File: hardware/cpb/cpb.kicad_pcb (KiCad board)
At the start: 6 copper layers, 95.9 x 90.2 mm, 5 parts, among them J1 Conn_02x20_Odd_Even

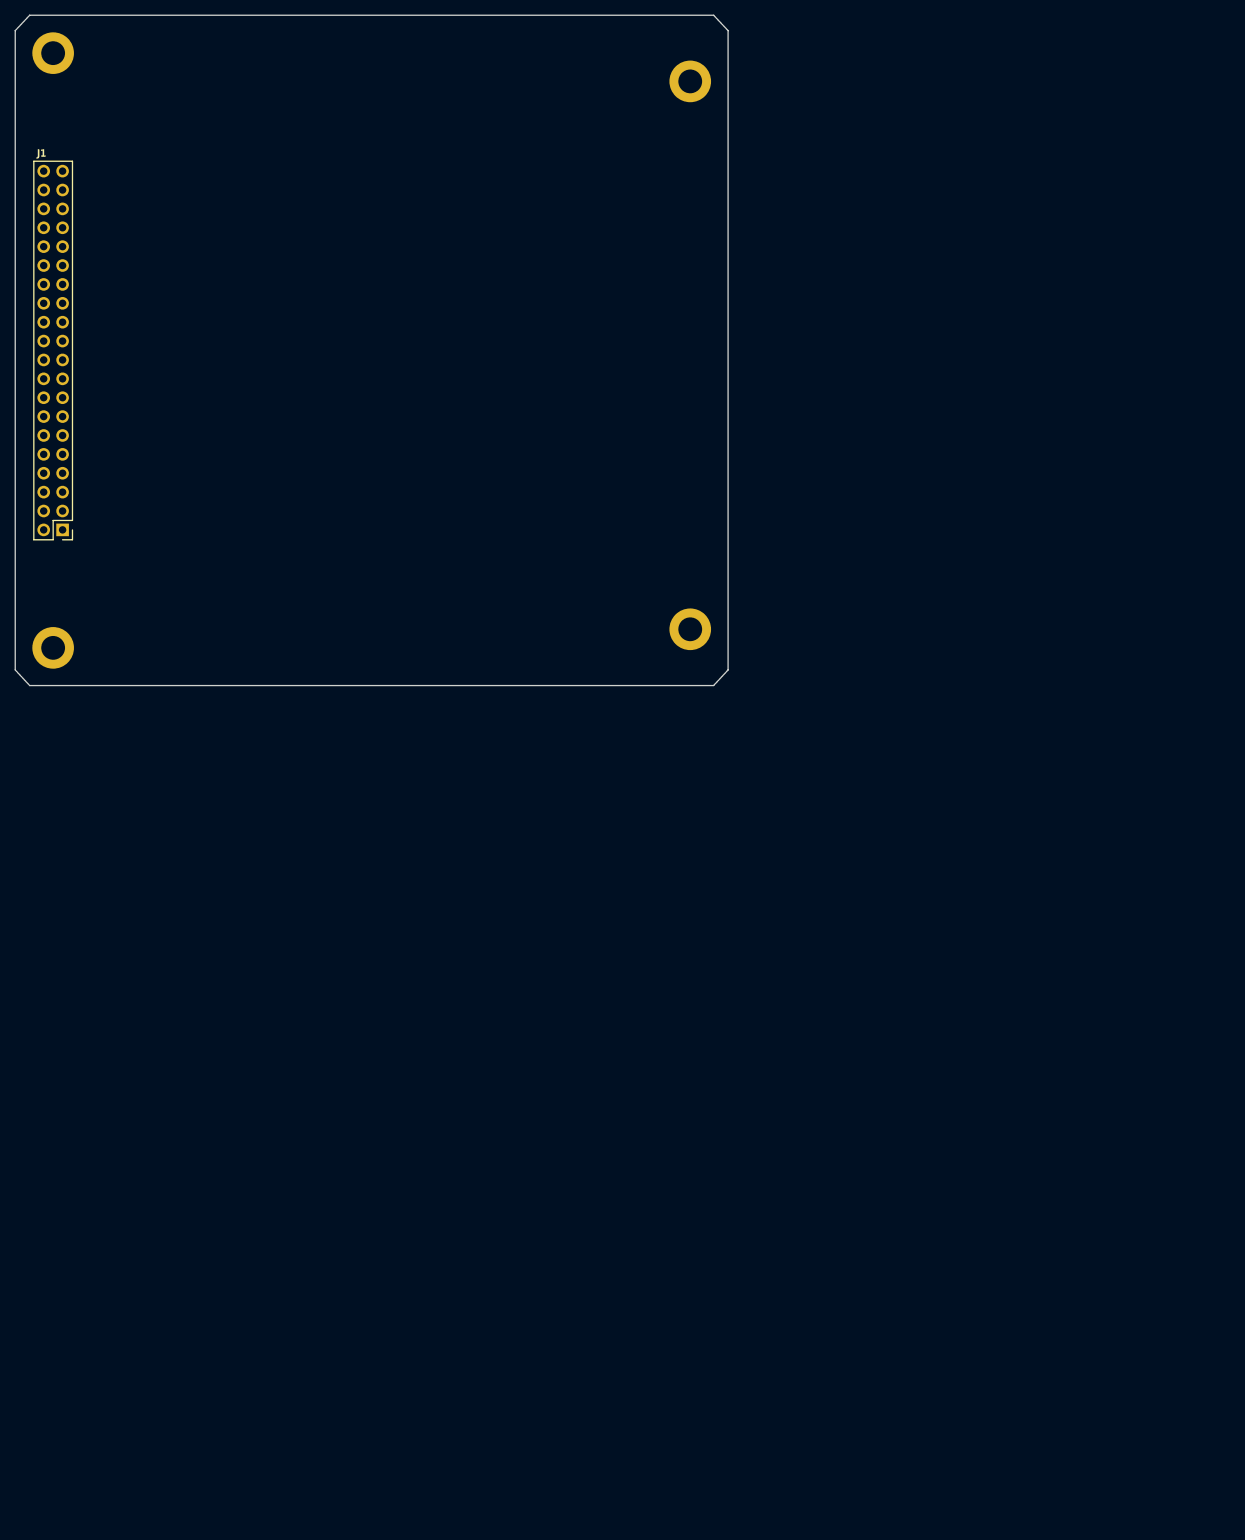
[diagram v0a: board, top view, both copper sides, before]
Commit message: hardware/cpb: Sorted initial ratsnest of CPB
This is the current revision of the sorted ratsnest of the CPB. Remaining tasks include placing down powerplanes as well as routing.
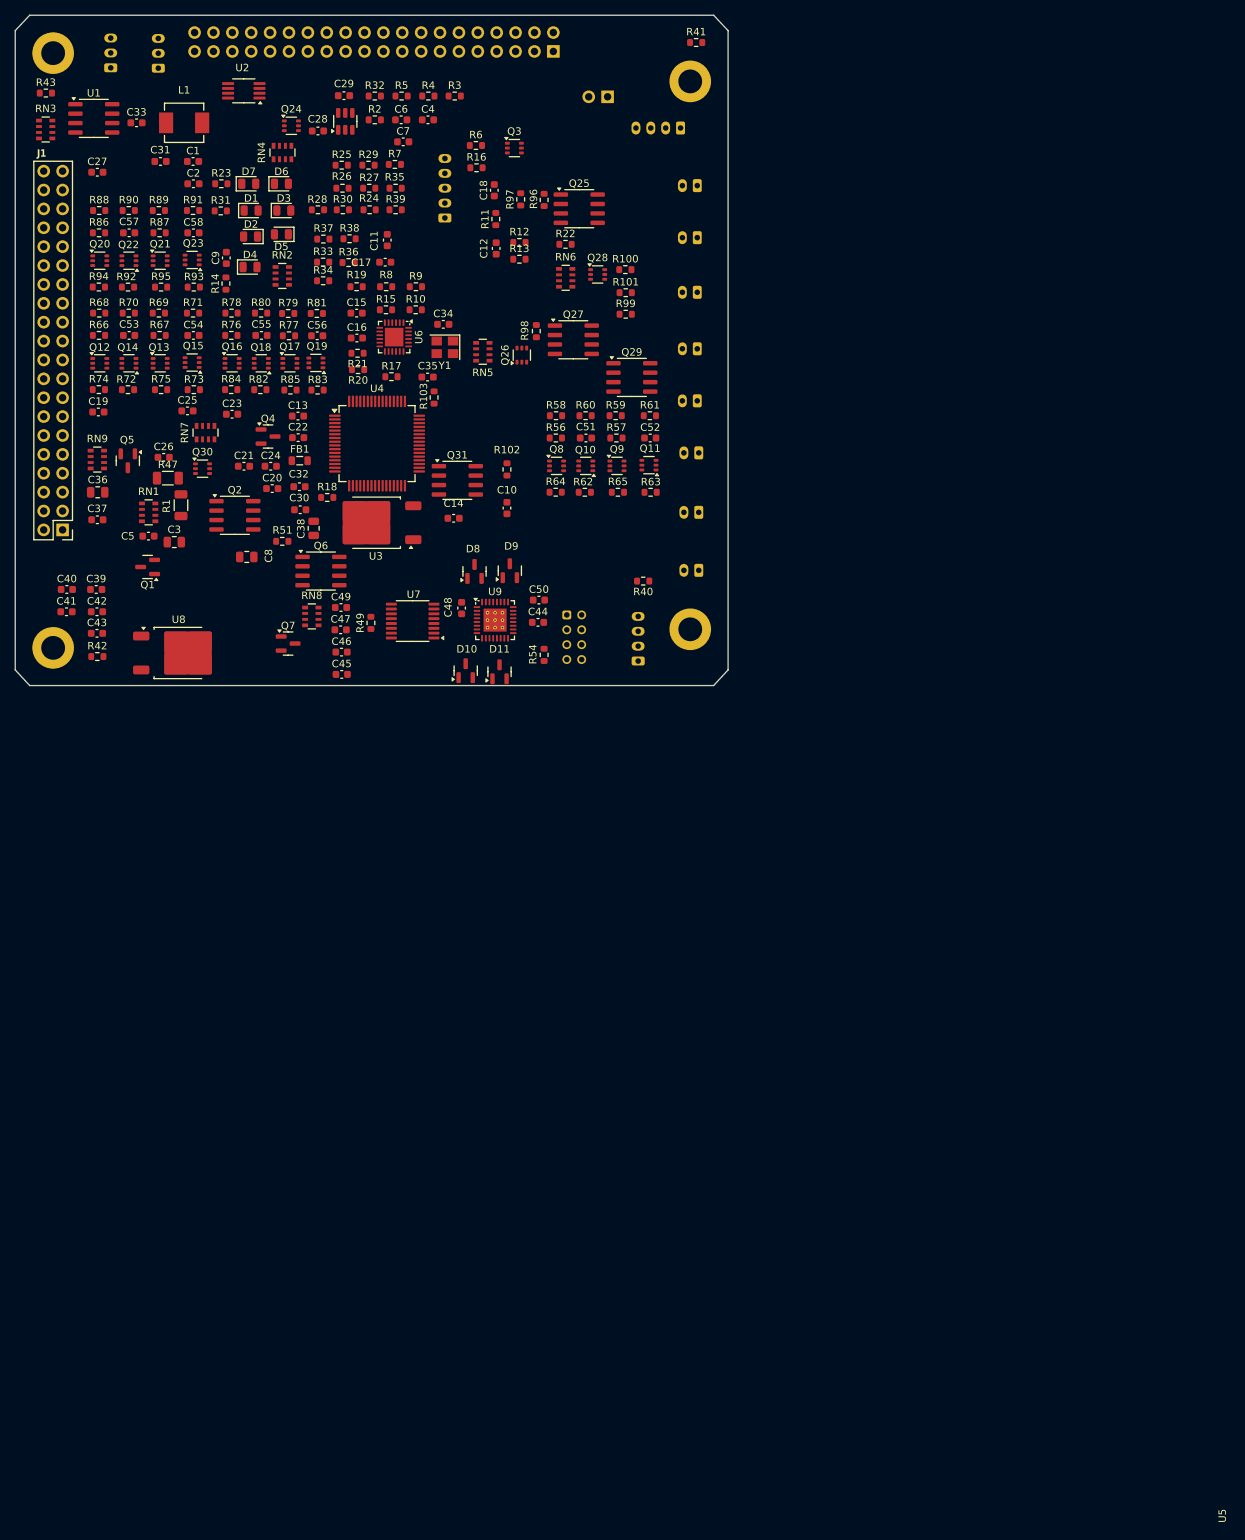
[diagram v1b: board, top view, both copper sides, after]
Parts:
- added C1: 100nF, Capacitor_SMD:C_0603_1608Metric, F.Cu at (124.8, 77.9)
- added C10: 2.2uF, Capacitor_SMD:C_0603_1608Metric, F.Cu at (167.0, 124.5)
- added C11: 68pF, Capacitor_SMD:C_0603_1608Metric, F.Cu at (150.9, 88.5)
- added C12: 68pF, Capacitor_SMD:C_0603_1608Metric, F.Cu at (165.6, 89.6)
- added C13: 100nF, Capacitor_SMD:C_0603_1608Metric, F.Cu at (138.9, 112.2)
- added C14: 100nF, Capacitor_SMD:C_0603_1608Metric, F.Cu at (159.8, 125.9)
- added C15: 100nF, Capacitor_SMD:C_0603_1608Metric, F.Cu at (146.8, 98.3)
- added C16: 100nF, Capacitor_SMD:C_0603_1608Metric, F.Cu at (146.8, 101.7)
- added C17: 10uF, Capacitor_SMD:C_0603_1608Metric, F.Cu at (150.6, 91.5)
- added C18: 10uF, Capacitor_SMD:C_0603_1608Metric, F.Cu at (165.3, 81.8)
- added C19: 100nF, Capacitor_SMD:C_0603_1608Metric, F.Cu at (112.0, 111.6)
- added C2: 100nF, Capacitor_SMD:C_0603_1608Metric, F.Cu at (124.8, 80.9)
- added C20: 100nF, Capacitor_SMD:C_0603_1608Metric, F.Cu at (135.4, 121.9)
- added C21: 100nF, Capacitor_SMD:C_0603_1608Metric, F.Cu at (131.6, 118.9)
- added C22: 100nF, Capacitor_SMD:C_0603_1608Metric, F.Cu at (138.9, 115.0)
- added C23: 100nF, Capacitor_SMD:C_0603_1608Metric, F.Cu at (130.0, 111.9)
- added C24: 100nF, Capacitor_SMD:C_0603_1608Metric, F.Cu at (135.2, 118.9)
- added C25: 100nF, Capacitor_SMD:C_0603_1608Metric, F.Cu at (124.0, 111.5)
- added C26: 100nF, Capacitor_SMD:C_0603_1608Metric, F.Cu at (120.8, 117.7)
- added C27: 100nF, Capacitor_SMD:C_0603_1608Metric, F.Cu at (111.9, 79.3)
- added C28: 2.2uF, Capacitor_SMD:C_0603_1608Metric, F.Cu at (141.6, 73.8)
- added C29: 100nF, Capacitor_SMD:C_0603_1608Metric, F.Cu at (145.1, 69.0)
- added C3: 22uF, Capacitor_SMD:C_0805_2012Metric, F.Cu at (122.2, 129.1)
- added C30: 100nF, Capacitor_SMD:C_0603_1608Metric, F.Cu at (139.2, 124.8)
- added C31: 2.2uF, Capacitor_SMD:C_0603_1608Metric, F.Cu at (120.4, 77.9)
- added C32: 2.2uF, Capacitor_SMD:C_0603_1608Metric, F.Cu at (139.1, 121.7)
- added C33: 100nF, Capacitor_SMD:C_0603_1608Metric, F.Cu at (117.2, 72.7)
- added C34: 22pF, Capacitor_SMD:C_0603_1608Metric, F.Cu at (158.4, 99.8)
- added C35: 15pF, Capacitor_SMD:C_0603_1608Metric, F.Cu at (156.3, 106.9)
- added C36: 22uF, Capacitor_SMD:C_0805_2012Metric, F.Cu at (112.0, 122.4)
- added C37: 2.2uF, Capacitor_SMD:C_0603_1608Metric, F.Cu at (111.9, 126.1)
- added C38: 22uF, Capacitor_SMD:C_0805_2012Metric, F.Cu at (141.0, 127.2)
- added C39: 2.2uF, Capacitor_SMD:C_0603_1608Metric, F.Cu at (111.8, 135.5)
- added C4: 100nF, Capacitor_SMD:C_0603_1608Metric, F.Cu at (156.4, 72.3)
- added C40: 100nF, Capacitor_SMD:C_0603_1608Metric, F.Cu at (107.8, 135.5)
- added C41: 100nF, Capacitor_SMD:C_0603_1608Metric, F.Cu at (107.8, 138.5)
- added C42: 100nF, Capacitor_SMD:C_0603_1608Metric, F.Cu at (111.8, 138.5)
- added C43: 100nF, Capacitor_SMD:C_0603_1608Metric, F.Cu at (111.8, 141.4)
- added C44: 2.2uF, Capacitor_SMD:C_0603_1608Metric, F.Cu at (171.2, 139.9)
- added C45: 100nF, Capacitor_SMD:C_0603_1608Metric, F.Cu at (144.8, 146.9)
- added C46: 100nF, Capacitor_SMD:C_0603_1608Metric, F.Cu at (144.8, 143.9)
- added C47: 100nF, Capacitor_SMD:C_0603_1608Metric, F.Cu at (144.6, 140.9)
- added C48: 1.0uF, Capacitor_SMD:C_0603_1608Metric, F.Cu at (160.9, 138.0)
- added C49: 100nF, Capacitor_SMD:C_0603_1608Metric, F.Cu at (144.7, 137.9)
- added C5: 2.2uF, Capacitor_SMD:C_0603_1608Metric, F.Cu at (118.8, 128.3)
- added C50: 22nF, Capacitor_SMD:C_0603_1608Metric, F.Cu at (171.3, 136.9)
- added C51: 10nF, Capacitor_SMD:C_0603_1608Metric, F.Cu at (177.6, 115.1)
- added C52: 10nF, Capacitor_SMD:C_0603_1608Metric, F.Cu at (186.3, 115.1)
- added C53: 10nF, Capacitor_SMD:C_0603_1608Metric, F.Cu at (116.2, 101.3)
- added C54: 10nF, Capacitor_SMD:C_0603_1608Metric, F.Cu at (124.8, 101.3)
- added C55: 10nF, Capacitor_SMD:C_0603_1608Metric, F.Cu at (134.0, 101.3)
- added C56: 10nF, Capacitor_SMD:C_0603_1608Metric, F.Cu at (141.5, 101.3)
- added C57: 10nF, Capacitor_SMD:C_0603_1608Metric, F.Cu at (116.2, 87.5)
- added C58: 10nF, Capacitor_SMD:C_0603_1608Metric, F.Cu at (124.8, 87.5)
- added C6: 680pF, Capacitor_SMD:C_0603_1608Metric, F.Cu at (152.8, 72.3)
- added C7: 680pF, Capacitor_SMD:C_0603_1608Metric, F.Cu at (153.0, 75.3)
- added C8: 22uF, Capacitor_SMD:C_0805_2012Metric, F.Cu at (132.0, 131.1)
- added C9: 100nF, Capacitor_SMD:C_0603_1608Metric, F.Cu at (129.2, 90.9)
- added D1: 7V5, LED_SMD:LED_0805_2012Metric, F.Cu at (132.6, 84.5)
- added D10: MMBZ15VALT1G, Package_TO_SOT_SMD:SOT-23, F.Cu at (161.4, 146.4)
- added D11: MMBZ15VALT1G, Package_TO_SOT_SMD:SOT-23, F.Cu at (166.0, 146.6)
- added D2: 5V, LED_SMD:LED_0805_2012Metric, F.Cu at (132.5, 88.0)
- added D3: 3V3, LED_SMD:LED_0805_2012Metric, F.Cu at (137.0, 84.5)
- added D4: PI3V3, LED_SMD:LED_0805_2012Metric, F.Cu at (132.4, 92.1)
- added D5: GPLED, LED_SMD:LED_0805_2012Metric, F.Cu at (136.7, 87.7)
- added D6: μCLED, LED_SMD:LED_0805_2012Metric, F.Cu at (136.7, 80.9)
- added D7: PILED, LED_SMD:LED_0805_2012Metric, F.Cu at (132.3, 80.9)
- added D8: MMBZ15VALT1G, Package_TO_SOT_SMD:SOT-23, F.Cu at (162.6, 133.1)
- added D9: MMBZ15VALT1G, Package_TO_SOT_SMD:SOT-23, F.Cu at (167.4, 132.9)
- added FB1: BLM21BD272SN1L, Inductor_SMD:L_0805_2012Metric, F.Cu at (139.1, 118.2)
- added J10: SW1, Connector_JST:JST_PH_B2B-PH-K_1x02_P2.00mm_Vertical, B.Cu at (192.6, 81.2)
- added J11: SW2, Connector_JST:JST_PH_B2B-PH-K_1x02_P2.00mm_Vertical, B.Cu at (192.6, 88.2)
- added J12: SW3, Connector_JST:JST_PH_B2B-PH-K_1x02_P2.00mm_Vertical, B.Cu at (192.6, 95.5)
- added J13: PISW1, Connector_JST:JST_PH_B2B-PH-K_1x02_P2.00mm_Vertical, B.Cu at (192.6, 103.1)
- added J14: μSW1, Connector_JST:JST_PH_B2B-PH-K_1x02_P2.00mm_Vertical, B.Cu at (192.6, 110.1)
- added J15: μSW2, Connector_JST:JST_PH_B2B-PH-K_1x02_P2.00mm_Vertical, B.Cu at (192.8, 117.1)
- added J16: μSW3, Connector_JST:JST_PH_B2B-PH-K_1x02_P2.00mm_Vertical, B.Cu at (192.8, 125.1)
- added J17: μSW4, Connector_JST:JST_PH_B2B-PH-K_1x02_P2.00mm_Vertical, B.Cu at (192.8, 132.9)
- added J2: I2CExt, Connector_JST:JST_PH_B5B-PH-K_1x05_P2.00mm_Vertical, B.Cu at (158.7, 85.5)
- added J3: DAC1BUF, Connector_JST:JST_PH_B3B-PH-K_1x03_P2.00mm_Vertical, B.Cu at (120.1, 65.3)
- added J4: DAC2BUF, Connector_JST:JST_PH_B3B-PH-K_1x03_P2.00mm_Vertical, B.Cu at (113.7, 65.3)
- added J6: Conn_02x20_Odd_Even, Connector_PinHeader_2.54mm:PinHeader_2x20_P2.54mm_Vertical, B.Cu at (173.2, 63.1)
- added J7: ADC6/7, Connector_JST:JST_PH_B4B-PH-K_1x04_P2.00mm_Vertical, B.Cu at (184.7, 145.1)
- added J8: ADC2/3, Connector_JST:JST_PH_B4B-PH-K_1x04_P2.00mm_Vertical, B.Cu at (190.3, 73.4)
- added J9: 4FBRG, Connector_JST:JST_PHD_B8B-PHDSS_2x04_P2.00mm_Vertical, B.Cu at (175.1, 138.9)
- added J99: RBFJUMP, Connector_PinHeader_2.54mm:PinHeader_1x02_P2.54mm_Horizontal, B.Cu at (180.5, 69.2)
- added L1: 4.7uH, Inductor_SMD:L_Vishay_IHLP-2020, F.Cu at (123.6, 72.7)
- added Q1: PMBT2222A, Package_TO_SOT_SMD:SOT-23, F.Cu at (118.7, 132.4)
- added Q10: BSS138PS,115, Package_TO_SOT_SMD:SOT-363_SC-70-6, F.Cu at (177.6, 118.8)
- added Q11: BSS138PS,115, Package_TO_SOT_SMD:SOT-363_SC-70-6, F.Cu at (186.1, 118.8)
- added Q12: MBT2222ADW1T1, Package_TO_SOT_SMD:SOT-363_SC-70-6, F.Cu at (112.2, 105.0)
- added Q13: MBT2222ADW1T1, Package_TO_SOT_SMD:SOT-363_SC-70-6, F.Cu at (120.3, 105.0)
- added Q14: BSS138PS,115, Package_TO_SOT_SMD:SOT-363_SC-70-6, F.Cu at (116.2, 105.0)
- added Q15: BSS138PS,115, Package_TO_SOT_SMD:SOT-363_SC-70-6, F.Cu at (124.7, 105.0)
- added Q16: MBT2222ADW1T1, Package_TO_SOT_SMD:SOT-363_SC-70-6, F.Cu at (130.0, 105.0)
- added Q17: MBT2222ADW1T1, Package_TO_SOT_SMD:SOT-363_SC-70-6, F.Cu at (137.8, 105.0)
- added Q18: BSS138PS,115, Package_TO_SOT_SMD:SOT-363_SC-70-6, F.Cu at (133.9, 105.0)
- added Q19: BSS138PS,115, Package_TO_SOT_SMD:SOT-363_SC-70-6, F.Cu at (141.3, 105.0)
- added Q2: IRF9393, Package_SO:SOIC-8_3.9x4.9mm_P1.27mm, F.Cu at (130.4, 125.5)
- added Q20: MBT2222ADW1T1, Package_TO_SOT_SMD:SOT-363_SC-70-6, F.Cu at (112.2, 91.2)
- added Q21: MBT2222ADW1T1, Package_TO_SOT_SMD:SOT-363_SC-70-6, F.Cu at (120.3, 91.2)
- added Q22: BSS138PS,115, Package_TO_SOT_SMD:SOT-363_SC-70-6, F.Cu at (116.2, 91.2)
- added Q23: BSS138PS,115, Package_TO_SOT_SMD:SOT-363_SC-70-6, F.Cu at (124.7, 91.2)
- added Q24: MBT2222ADW1T1, Package_TO_SOT_SMD:SOT-363_SC-70-6, F.Cu at (138.0, 73.1)
- added Q25: IRF7306, Package_SO:SOIC-8_3.9x4.9mm_P1.27mm, F.Cu at (176.7, 84.3)
- added Q26: MBT2222ADW1T1, Package_TO_SOT_SMD:SOT-363_SC-70-6, F.Cu at (169.0, 104.0)
- added Q27: IRF7306, Package_SO:SOIC-8_3.9x4.9mm_P1.27mm, F.Cu at (175.9, 101.9)
- added Q28: MBT2222ADW1T1, Package_TO_SOT_SMD:SOT-363_SC-70-6, F.Cu at (179.2, 93.1)
- added Q29: IRF7306, Package_SO:SOIC-8_3.9x4.9mm_P1.27mm, F.Cu at (183.8, 107.0)
- added Q3: MBT2222ADW1T1, Package_TO_SOT_SMD:SOT-363_SC-70-6, F.Cu at (168.0, 76.1)
- added Q30: MBT2222ADW1T1, Package_TO_SOT_SMD:SOT-363_SC-70-6, F.Cu at (126.0, 119.2)
- added Q31: IRF7306, Package_SO:SOIC-8_3.9x4.9mm_P1.27mm, F.Cu at (160.3, 120.8)
- added Q4: PMBT2222A, Package_TO_SOT_SMD:SOT-23, F.Cu at (134.9, 114.9)
- added Q5: PMBT2222A, Package_TO_SOT_SMD:SOT-23, F.Cu at (116.0, 118.2)
- added Q6: IRF9393, Package_SO:SOIC-8_3.9x4.9mm_P1.27mm, F.Cu at (142.0, 133.0)
- added Q7: PMBT2222A, Package_TO_SOT_SMD:SOT-23, F.Cu at (137.6, 142.8)
- added Q8: MBT2222ADW1T1, Package_TO_SOT_SMD:SOT-363_SC-70-6, F.Cu at (173.7, 118.8)
- added Q9: MBT2222ADW1T1, Package_TO_SOT_SMD:SOT-363_SC-70-6, F.Cu at (181.8, 118.8)
- added R1: 200m 1W, Resistor_SMD:R_1206_3216Metric, F.Cu at (123.2, 124.1)
- added R10: 5.6k, Resistor_SMD:R_0603_1608Metric, F.Cu at (154.7, 97.8)
- added R100: 10k, Resistor_SMD:R_0603_1608Metric, F.Cu at (182.9, 92.5)
- added R101: 10k, Resistor_SMD:R_0603_1608Metric, F.Cu at (183.0, 95.5)
- added R102: 10k, Resistor_SMD:R_0603_1608Metric, F.Cu at (167.0, 119.3)
- added R103: 10k, Resistor_SMD:R_0603_1608Metric, F.Cu at (157.2, 109.7)
- added R11: 0, Resistor_SMD:R_0603_1608Metric, F.Cu at (165.5, 85.7)
- added R12: 3.3k, Resistor_SMD:R_0603_1608Metric, F.Cu at (168.7, 88.8)
- added R13: 5.6k, Resistor_SMD:R_0603_1608Metric, F.Cu at (168.7, 91.0)
- added R14: 1k, Resistor_SMD:R_0603_1608Metric, F.Cu at (129.2, 94.3)
- added R15: 0, Resistor_SMD:R_0603_1608Metric, F.Cu at (150.7, 97.8)
- added R16: 0, Resistor_SMD:R_0603_1608Metric, F.Cu at (162.9, 78.8)
- added R17: 10k, Resistor_SMD:R_0603_1608Metric, F.Cu at (151.5, 106.8)
- added R18: 33, Resistor_SMD:R_0603_1608Metric, F.Cu at (142.8, 123.1)
- added R19: 10k, Resistor_SMD:R_0603_1608Metric, F.Cu at (146.8, 94.8)
- added R2: 3.3k, Resistor_SMD:R_0603_1608Metric, F.Cu at (149.2, 72.3)
- added R20: 4.7k, Resistor_SMD:R_0603_1608Metric, F.Cu at (147.0, 105.9)
- added R21: 4.7k, Resistor_SMD:R_0603_1608Metric, F.Cu at (146.9, 103.7)
- added R22: 5.6k, Resistor_SMD:R_0603_1608Metric, F.Cu at (174.9, 89.0)
- added R23: 3.3k, Resistor_SMD:R_0603_1608Metric, F.Cu at (128.6, 80.9)
- added R24: 10k, Resistor_SMD:R_0603_1608Metric, F.Cu at (148.5, 84.4)
- added R25: 10k, Resistor_SMD:R_0603_1608Metric, F.Cu at (144.8, 78.4)
- added R26: 10k, Resistor_SMD:R_0603_1608Metric, F.Cu at (144.9, 81.5)
- added R27: 10k, Resistor_SMD:R_0603_1608Metric, F.Cu at (148.5, 81.5)
- added R28: 1.5k, Resistor_SMD:R_0603_1608Metric, F.Cu at (141.6, 84.4)
- added R29: 33, Resistor_SMD:R_0603_1608Metric, F.Cu at (148.4, 78.4)
- added R3: 3.3k, Resistor_SMD:R_0603_1608Metric, F.Cu at (160.0, 69.1)
- added R30: 33, Resistor_SMD:R_0603_1608Metric, F.Cu at (144.9, 84.4)
- added R31: 10k, Resistor_SMD:R_0603_1608Metric, F.Cu at (128.5, 84.5)
- added R32: 10k, Resistor_SMD:R_0603_1608Metric, F.Cu at (149.2, 69.1)
- added R33: 10k, Resistor_SMD:R_0603_1608Metric, F.Cu at (142.3, 91.4)
- added R34: 10k, Resistor_SMD:R_0603_1608Metric, F.Cu at (142.3, 94.0)
- added R35: 10k, Resistor_SMD:R_0603_1608Metric, F.Cu at (152.0, 81.5)
- added R36: 10k, Resistor_SMD:R_0603_1608Metric, F.Cu at (145.7, 91.5)
- added R37: 33, Resistor_SMD:R_0603_1608Metric, F.Cu at (142.3, 88.3)
- added R38: 33, Resistor_SMD:R_0603_1608Metric, F.Cu at (145.8, 88.3)
- added R39: 10k, Resistor_SMD:R_0603_1608Metric, F.Cu at (152.0, 84.4)
- added R4: 5.6k, Resistor_SMD:R_0603_1608Metric, F.Cu at (156.4, 69.1)
- added R40: 33, Resistor_SMD:R_0603_1608Metric, F.Cu at (185.3, 134.3)
- added R41: 33, Resistor_SMD:R_0603_1608Metric, F.Cu at (192.4, 61.9)
- added R42: 33, Resistor_SMD:R_0603_1608Metric, F.Cu at (111.9, 144.5)
- added R43: 33, Resistor_SMD:R_0603_1608Metric, F.Cu at (105.0, 68.7)
- added R47: 200m 1W, Resistor_SMD:R_1206_3216Metric, F.Cu at (121.4, 120.5)
- added R49: 10k, Resistor_SMD:R_0603_1608Metric, F.Cu at (148.7, 140.0)
- added R5: 9.1k, Resistor_SMD:R_0603_1608Metric, F.Cu at (152.8, 69.1)
- added R51: 10k, Resistor_SMD:R_0603_1608Metric, F.Cu at (136.8, 129.0)
- added R54: 15k, Resistor_SMD:R_0603_1608Metric, F.Cu at (172.0, 144.3)
- added R56: 680, Resistor_SMD:R_0603_1608Metric, F.Cu at (173.6, 115.1)
- added R57: 680, Resistor_SMD:R_0603_1608Metric, F.Cu at (181.7, 115.1)
- added R58: 10k, Resistor_SMD:R_0603_1608Metric, F.Cu at (173.6, 112.1)
- added R59: 10k, Resistor_SMD:R_0603_1608Metric, F.Cu at (181.6, 112.1)
- added R6: 5.6k, Resistor_SMD:R_0603_1608Metric, F.Cu at (162.8, 75.8)
- added R60: 100k, Resistor_SMD:R_0603_1608Metric, F.Cu at (177.6, 112.1)
- added R61: 100k, Resistor_SMD:R_0603_1608Metric, F.Cu at (186.2, 112.1)
- added R62: 200k, Resistor_SMD:R_0603_1608Metric, F.Cu at (177.5, 122.4)
- added R63: 200k, Resistor_SMD:R_0603_1608Metric, F.Cu at (186.3, 122.4)
- added R64: 6.8k, Resistor_SMD:R_0603_1608Metric, F.Cu at (173.6, 122.4)
- added R65: 6.8k, Resistor_SMD:R_0603_1608Metric, F.Cu at (181.9, 122.4)
- added R66: 680, Resistor_SMD:R_0603_1608Metric, F.Cu at (112.1, 101.3)
- added R67: 680, Resistor_SMD:R_0603_1608Metric, F.Cu at (120.3, 101.3)
- added R68: 10k, Resistor_SMD:R_0603_1608Metric, F.Cu at (112.2, 98.3)
- added R69: 10k, Resistor_SMD:R_0603_1608Metric, F.Cu at (120.2, 98.3)
- added R7: 9.1k, Resistor_SMD:R_0603_1608Metric, F.Cu at (151.9, 78.3)
- added R70: 100k, Resistor_SMD:R_0603_1608Metric, F.Cu at (116.1, 98.3)
- added R71: 100k, Resistor_SMD:R_0603_1608Metric, F.Cu at (124.8, 98.3)
- added R72: 200k, Resistor_SMD:R_0603_1608Metric, F.Cu at (116.0, 108.6)
- added R73: 200k, Resistor_SMD:R_0603_1608Metric, F.Cu at (124.9, 108.6)
- added R74: 6.8k, Resistor_SMD:R_0603_1608Metric, F.Cu at (112.1, 108.6)
- added R75: 6.8k, Resistor_SMD:R_0603_1608Metric, F.Cu at (120.5, 108.6)
- added R76: 680, Resistor_SMD:R_0603_1608Metric, F.Cu at (129.9, 101.3)
- added R77: 680, Resistor_SMD:R_0603_1608Metric, F.Cu at (137.7, 101.3)
- added R78: 10k, Resistor_SMD:R_0603_1608Metric, F.Cu at (129.9, 98.3)
- added R79: 10k, Resistor_SMD:R_0603_1608Metric, F.Cu at (137.6, 98.3)
- added R8: 0, Resistor_SMD:R_0603_1608Metric, F.Cu at (150.8, 94.8)
- added R80: 100k, Resistor_SMD:R_0603_1608Metric, F.Cu at (133.9, 98.3)
- added R81: 100k, Resistor_SMD:R_0603_1608Metric, F.Cu at (141.4, 98.3)
- added R82: 200k, Resistor_SMD:R_0603_1608Metric, F.Cu at (133.8, 108.6)
- added R83: 200k, Resistor_SMD:R_0603_1608Metric, F.Cu at (141.5, 108.7)
- added R84: 6.8k, Resistor_SMD:R_0603_1608Metric, F.Cu at (129.9, 108.6)
- added R85: 6.8k, Resistor_SMD:R_0603_1608Metric, F.Cu at (137.9, 108.7)
- added R86: 680, Resistor_SMD:R_0603_1608Metric, F.Cu at (112.1, 87.5)
- added R87: 680, Resistor_SMD:R_0603_1608Metric, F.Cu at (120.3, 87.5)
- added R88: 10k, Resistor_SMD:R_0603_1608Metric, F.Cu at (112.2, 84.5)
- added R89: 10k, Resistor_SMD:R_0603_1608Metric, F.Cu at (120.2, 84.5)
- added R9: 3.3k, Resistor_SMD:R_0603_1608Metric, F.Cu at (154.8, 94.8)
- added R90: 100k, Resistor_SMD:R_0603_1608Metric, F.Cu at (116.1, 84.5)
- added R91: 100k, Resistor_SMD:R_0603_1608Metric, F.Cu at (124.8, 84.5)
- added R92: 200k, Resistor_SMD:R_0603_1608Metric, F.Cu at (116.0, 94.8)
- added R93: 200k, Resistor_SMD:R_0603_1608Metric, F.Cu at (124.9, 94.8)
- added R94: 6.8k, Resistor_SMD:R_0603_1608Metric, F.Cu at (112.1, 94.8)
- added R95: 6.8k, Resistor_SMD:R_0603_1608Metric, F.Cu at (120.5, 94.8)
- added R96: 10k, Resistor_SMD:R_0603_1608Metric, F.Cu at (172.0, 83.1)
- added R97: 10k, Resistor_SMD:R_0603_1608Metric, F.Cu at (168.8, 83.0)
- added R98: 10k, Resistor_SMD:R_0603_1608Metric, F.Cu at (170.9, 100.7)
- added R99: 10k, Resistor_SMD:R_0603_1608Metric, F.Cu at (183.0, 98.5)
- added RN1: 4.7k, Resistor_SMD:R_Array_Convex_4x0603, F.Cu at (118.8, 125.1)
- added RN2: 1.5k, Resistor_SMD:R_Array_Convex_4x0603, F.Cu at (136.8, 93.3)
- added RN3: 3.3k, Resistor_SMD:R_Array_Convex_4x0603, F.Cu at (105.0, 73.6)
- added RN4: 4.7k, Resistor_SMD:R_Array_Convex_4x0603, F.Cu at (136.8, 76.7)
- added RN5: 4.7k, Resistor_SMD:R_Array_Convex_4x0603, F.Cu at (163.8, 103.5)
- added RN6: 4.7k, Resistor_SMD:R_Array_Convex_4x0603, F.Cu at (174.9, 93.5)
- added RN7: 4.7k, Resistor_SMD:R_Array_Convex_4x0603, F.Cu at (126.5, 114.4)
- added RN8: 10k, Resistor_SMD:R_Array_Convex_4x0603, F.Cu at (140.8, 139.1)
- added RN9: 4.7k, Resistor_SMD:R_Array_Convex_4x0603, F.Cu at (111.9, 118.0)
- added U1: TS912, Package_SO:SOIC-8_3.9x4.9mm_P1.27mm, F.Cu at (111.4, 72.1)
- added U2: ADR420ARMZ, Package_SO:MSOP-8_3x3mm_P0.65mm, F.Cu at (131.6, 68.4)
- added U3: KF33BDT, Package_TO_SOT_SMD:TO-252-2, F.Cu at (149.4, 126.5)
- added U4: STM32L072R_B-Z_Tx, Package_QFP:LQFP-64_10x10mm_P0.5mm, F.Cu at (149.5, 115.8)
- added U5: AP63205WU, Package_TO_SOT_SMD:TSOT-23-6, F.Cu at (145.2, 72.5)
- added U6: SC16IS750xBS, Package_DFN_QFN:HVQFN-24-1EP_4x4mm_P0.5mm_EP2.5x2.5mm, F.Cu at (151.8, 101.5)
- added U7: SC18IS606, Package_SO:TSSOP-16_4.4x5mm_P0.65mm, F.Cu at (154.3, 139.7)
- added U8: KF33BDT, Package_TO_SOT_SMD:TO-252-2, F.Cu at (122.8, 144.0)
- added U9: MAX22200, Package_DFN_QFN:QFN-32-1EP_5x5mm_P0.5mm_EP3.1x3.1mm_ThermalVias, F.Cu at (165.4, 139.6)
- added Y1: 14.7456MHz, Crystal:Crystal_SMD_3225-4Pin_3.2x2.5mm, F.Cu at (158.7, 102.9)
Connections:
- H1 pad 1: (no net) -> Net-(H1-Pad1)
- H2 pad 1: (no net) -> Net-(H2-Pad1)
- H3 pad 1: (no net) -> Net-(H3-Pad1)
- H4 pad 1: (no net) -> Net-(H4-Pad1)
- J1 pad 1: (no net) -> +BATT
- J1 pad 10: (no net) -> GND
- J1 pad 11: (no net) -> unconnected-(J1-Pin_11-Pad11)
- J1 pad 12: (no net) -> GND
- J1 pad 13: (no net) -> unconnected-(J1-Pin_13-Pad13)
- J1 pad 14: (no net) -> GND
- J1 pad 15: (no net) -> unconnected-(J1-Pin_15-Pad15)
- J1 pad 16: (no net) -> GND
- J1 pad 17: (no net) -> /SDA
- J1 pad 18: (no net) -> GND
- J1 pad 19: (no net) -> /SCL
- J1 pad 2: (no net) -> GND
- J1 pad 20: (no net) -> GND
- J1 pad 21: (no net) -> /PRIPWREN
- J1 pad 22: (no net) -> GND
- J1 pad 23: (no net) -> /FBRGPWREN
- J1 pad 24: (no net) -> GND
- J1 pad 25: (no net) -> unconnected-(J1-Pin_25-Pad25)
- J1 pad 26: (no net) -> GND
- J1 pad 27: (no net) -> unconnected-(J1-Pin_27-Pad27)
- J1 pad 28: (no net) -> GND
- J1 pad 29: (no net) -> unconnected-(J1-Pin_29-Pad29)
- J1 pad 3: (no net) -> +BATT
- J1 pad 30: (no net) -> GND
- J1 pad 31: (no net) -> unconnected-(J1-Pin_31-Pad31)
- J1 pad 32: (no net) -> GND
- J1 pad 33: (no net) -> unconnected-(J1-Pin_33-Pad33)
- J1 pad 34: (no net) -> GND
- J1 pad 36: (no net) -> GND
- J1 pad 37: (no net) -> Net-(J1-Pin_37)
- J1 pad 38: (no net) -> GND
- J1 pad 39: (no net) -> Net-(J1-Pin_37)
- J1 pad 4: (no net) -> GND
- J1 pad 40: (no net) -> GND
- J1 pad 5: (no net) -> +BATT
- J1 pad 6: (no net) -> GND
- J1 pad 7: (no net) -> +BATT
- J1 pad 8: (no net) -> GND
- J1 pad 9: (no net) -> +BATT

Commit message: hardware/cpb: Transistors on right sorted and bypass capacitors added Moved the transistors into groups then placed next to connectors and placed bypass capacitors near power pins.
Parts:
- moved RN7 62.2 mm to (186.3, 131.2), turned to 180 degrees
- moved C14 62.0 mm to (125.0, 74.6), turned to 0 degrees
- moved Q3 59.5 mm to (108.5, 73.7)
- moved Q30 57.7 mm to (182.6, 130.9), turned to 90 degrees
- moved U3 54.0 mm to (134.7, 74.5), turned to 0 degrees
- moved RN4 50.6 mm to (186.2, 87.7), turned to 180 degrees
- moved R18 47.3 mm to (141.6, 75.8), turned to 180 degrees
- moved Q24 46.7 mm to (182.4, 87.5), turned to 90 degrees
- moved R99 45.9 mm to (147.8, 127.8)
- moved C20 45.4 mm to (125.0, 77.7)
- moved C46 42.0 mm to (118.5, 111.2)
- moved C40 35.6 mm to (143.4, 133.8), turned to 180 degrees
- moved C25 33.2 mm to (115.6, 79.3)
- moved C41 31.7 mm to (139.4, 138.1)
- moved C42 31.5 mm to (143.4, 138.1)
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
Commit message: hardware/cpb: moved u6 and added bypass capacitors
Untangled components around u6 as well as flipped top right corner connectors. Bypass capacitors added for U1-U9.
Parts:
- moved C19 46.9 mm to (158.1, 120.7)
- moved C9 36.2 mm to (149.2, 121.1), turned to 180 degrees
- moved J2 32.3 mm to (185.6, 67.7), turned to 180 degrees
- moved C23 32.2 mm to (127.9, 79.8)
- moved C21 32.0 mm to (128.6, 87.0)
- moved C33 31.7 mm to (149.1, 75.3)
- moved C4 30.2 mm to (126.6, 67.1)
- moved C47 29.6 mm to (116.4, 111.6)
- moved C40 27.9 mm to (125.7, 112.2), turned to 0 degrees
- moved C24 24.2 mm to (112.4, 110.8)
- moved C41 23.3 mm to (127.3, 118.1), turned to -90 degrees
- moved C45 22.5 mm to (121.4, 111.9)
- moved R17 22.4 mm to (132.2, 95.3)
- moved C43 21.9 mm to (127.3, 121.6), turned to 90 degrees
- moved C42 20.8 mm to (127.3, 124.9), turned to 90 degrees
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
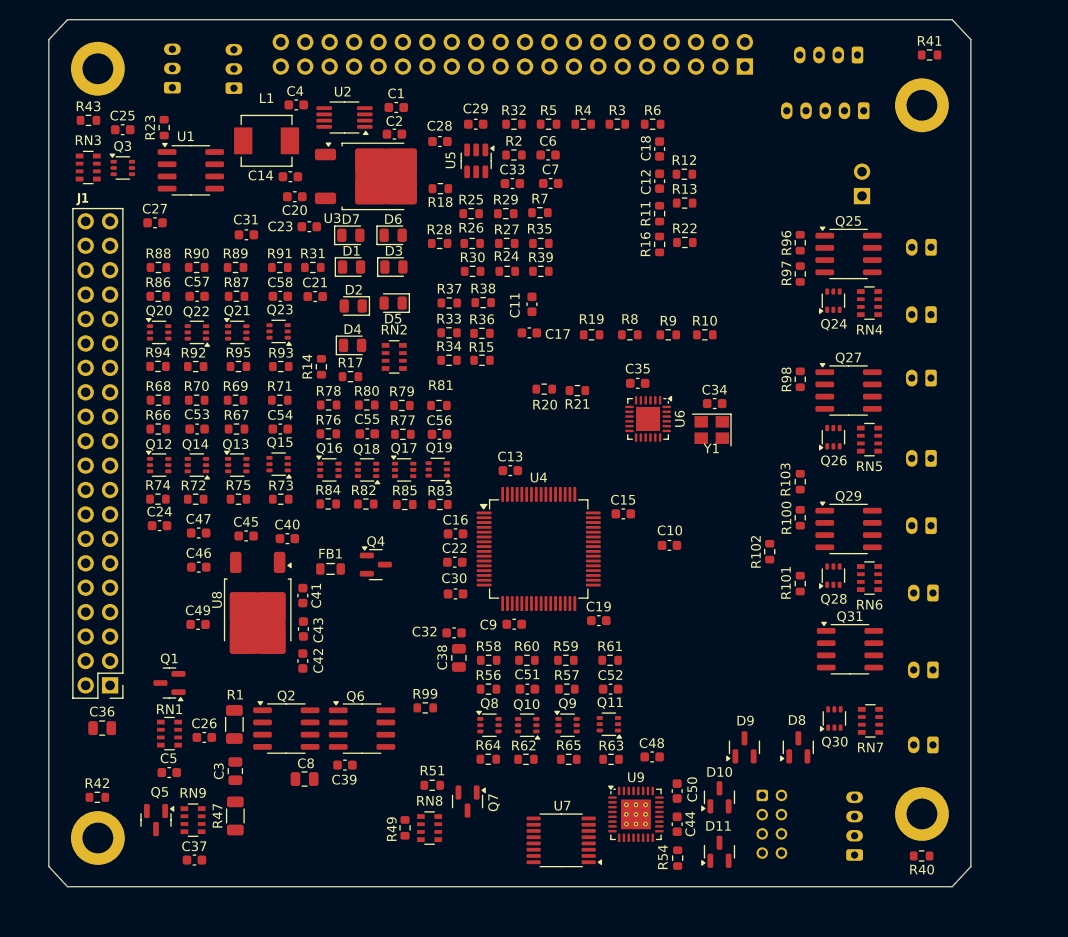
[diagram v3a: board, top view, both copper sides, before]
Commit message: cpb: many, many fixes
- Move components to bottom to match design intent
- Adjust AP62305 to hopefully have correct pinout
- Replace manual RBF jumper with solder jumper: just not enough room
- High level adjustment to placement to ease layout.
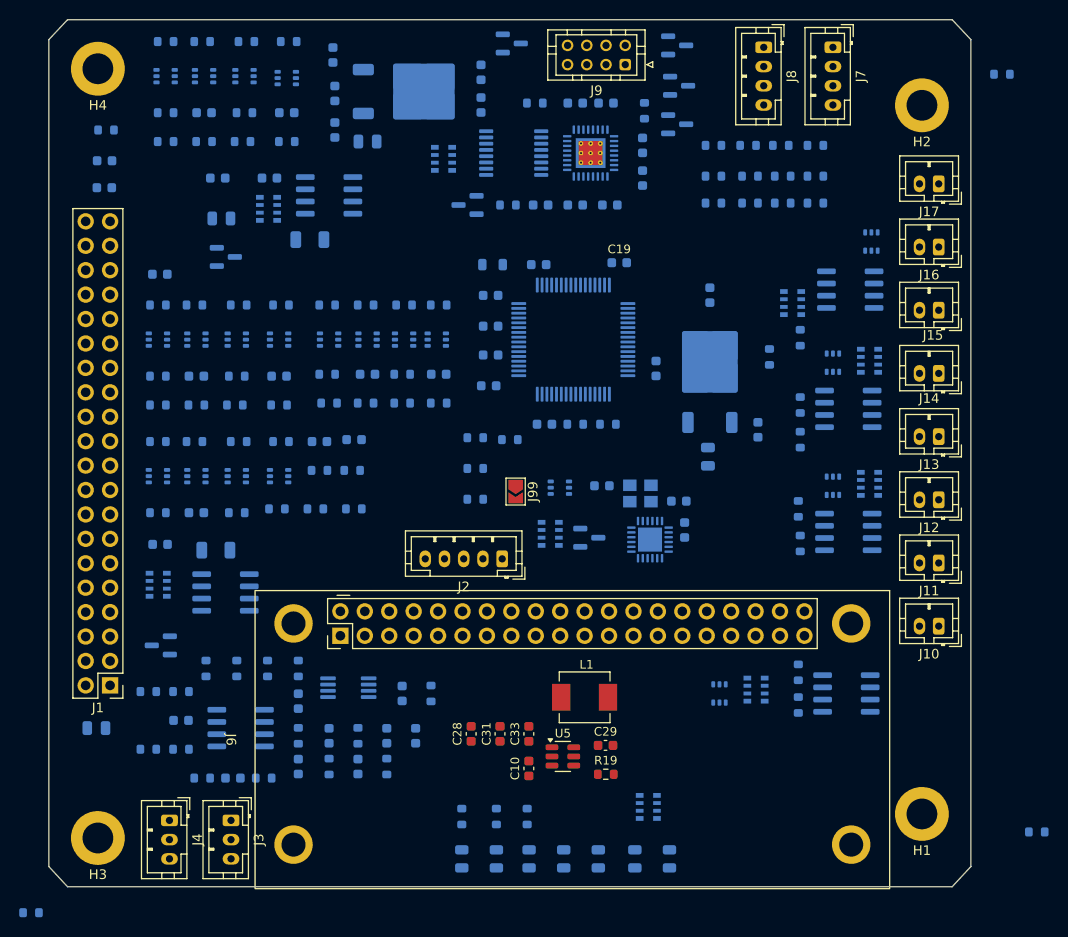
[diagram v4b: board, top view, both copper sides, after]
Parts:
- C1, C11, C12, C13, C14, C15, C16, C17, C18, C19, C2, C20, C21, C22, C23, C24, C25, C26, C27, C3, C30, C32, C34, C35, C36, C37, C38, C39, C4, C40, C41, C42, C43, C44, C45, C46, C47, C48, C49, C5, C50, C51, C52, C53, C54, C55, C56, C57, C58, C6, C7, C8, C9, D1, D10, D11, D2, D3, D4, D5, D6, D7, D8, D9, FB1, Q1, Q10, Q11, Q12, Q13, Q14, Q15, Q16, Q17, Q18, Q19, Q2, Q20, Q21, Q22, Q23, Q24, Q25, Q26, Q27, Q28, Q29, Q3, Q30, Q31, Q4, Q5, Q6, Q7, Q8, Q9, R1, R10, R100, R101, R102, R103, R11, R12, R13, R14, R15, R16, R17, R18, R2, R20, R21, R22, R23, R24, R25, R26, R27, R28, R29, R3, R30, R31, R32, R33, R34, R35, R36, R37, R38, R39, R4, R40, R41, R42, R43, R47, R49, R5, R51, R54, R56, R57, R58, R59, R6, R60, R61, R62, R63, R64, R65, R66, R67, R68, R69, R7, R70, R71, R72, R73, R74, R75, R76, R77, R78, R79, R8, R80, R81, R82, R83, R84, R85, R86, R87, R88, R89, R9, R90, R91, R92, R93, R94, R95, R96, R97, R98, R99, RN1, RN2, RN3, RN4, RN5, RN6, RN7, RN8, RN9, U1, U2, U3, U4, U6, U7, U8, U9, Y1: moved to B.Cu
- J10, J11, J12, J13, J14, J15, J16, J17, J2, J3, J4, J7, J8, J9: moved to F.Cu
- J6: footprint Connector_PinHeader_2.54mm:PinHeader_2x20_P2.54mm_Vertical -> SSE_Footprints:RPI02W; moved to F.Cu
- J99: footprint Connector_PinHeader_2.54mm:PinHeader_1x02_P2.54mm_Horizontal -> Jumper:SolderJumper-2_P1.3mm_Open_TrianglePad1.0x1.5mm; moved to F.Cu
- U5: value AP63205WU -> AP62301WU
- moved D11 86.8 mm to (149.0, 60.7), turned to 0 degrees
- moved J7 84.0 mm to (182.4, 61.1), turned to -90 degrees
- moved R62 81.9 mm to (116.8, 60.5)
- moved R64 81.8 mm to (113.0, 60.5)
- moved R65 81.8 mm to (121.4, 60.5)
- moved R63 81.8 mm to (125.8, 60.5)
- moved R23 79.5 mm to (147.4, 141.1), turned to -90 degrees
- moved C18 79.1 mm to (120.0, 137.1), turned to 180 degrees
- moved R54 77.8 mm to (162.8, 67.7), turned to 90 degrees
- moved J9 77.3 mm to (160.8, 62.9), turned to 180 degrees
- moved R49 76.6 mm to (151.4, 66.9), turned to 0 degrees
- moved J4 76.2 mm to (113.4, 141.5), turned to -90 degrees
- moved J3 76.2 mm to (119.8, 141.5), turned to -90 degrees
- moved Q8 75.4 mm to (113.0, 64.1)
- moved Q10 75.4 mm to (117.0, 64.1)
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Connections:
- U5 pad 1: +5V -> GND
- U5 pad 2: /EN5V -> Net-(U5-SW)
- U5 pad 4: GND -> +5V
- U5 pad 5: Net-(U5-SW) -> /EN5V
